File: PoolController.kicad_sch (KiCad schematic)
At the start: 18 parts, among them J1 RJ12, J2 RJ12, J3 Header, J4 Conn_02x12_Counter_Clockwise, Q1 MMBT3904, U1 LM2678S-5.0/NOPB

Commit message: Add revision 15 RX clamp and TX drive prototype package
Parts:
- added D3: BAT54, Package_TO_SOT_SMD:SOT-23, symbol PoolController:BAT54
- J1, J2: footprint Connector_RJ:RJ25_RJ12_5324_mini -> PoolController:RJ12_5324_6P6C
- L1: MPN NPI105C121MTRF or SRR1050A-121Y -> SRR1050A-121Y; Manufacturer NIC Components or Bournes Inc. -> Bourns
- R3: value R1k -> R560; MPN RC0603FR-071KL -> RC0603FR-07560RL
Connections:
- net RX: now reaches J3.2 (Pin_2), J4.5 (Pin_5), R1.2, R2.1
- net RX: now also D3.1 (A)
- net +3V3_MODULE: now reaches J4.3 (Pin_3)
- net +3V3_MODULE: now also D3.3 (K)
- no-connect marks 22 -> 21
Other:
- note added: "RX protection (issue #3) Cathode to Waveshare 3V3 (J4.3). Module must be fitted and powered. Validate powered-off / rail-injection behavior."
- note removed: "+5v"
- note removed: "GND"
- note removed: "RX"
- note removed: "TX"
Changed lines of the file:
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@@
 	(title_block
 		(title "Connect 10 Controller")
-		(date "2026-08-01")
-		(rev "14")
-	)
-	(text "+5v"
-		(exclude_from_sim no)
-		(at 141.478 83.82 0)
-		(effects
-			(font
-				(size 1.27 1.27)
-			)
-		)
-	)
-	(text "GND"
-		(exclude_from_sim no)
-		(at 141.224 86.614 0)
-		(effects
-			(font
-				(size 1.27 1.27)
-			)
-		)
-	)
-	(text "TX"
-		(exclude_from_sim no)
-		(at 142.24 96.774 0)
-		(effects
-			(font
-				(size 1.27 1.27)
-			)
-		)
-	)
-	(text "RX"
-		(exclude_from_sim no)
-		(at 142.24 94.234 0)
-		(effects
-			(font
-				(size 1.27 1.27)
-			)
-		)
+		(date "2026-09-12")
+		(rev "15")
 	)
 	(junction
@@
 	)
 	(no_connect
-		(at 148.59 93.98)
-	)
-	(no_connect
 		(at 161.29 93.98)
 	)
@@
 			)
 		)
-		(property "MPN" "NPI105C121MTRF or SRR1050A-121Y"
+		(property "MPN" "SRR1050A-121Y"
 			(at 138.43 62.23 0)
 			(effects
@@
 			)
 		)
-		(property "Manufacturer" "NIC Components or Bournes Inc."
+		(property "Manufacturer" "Bourns"
 			(at 138.43 62.23 0)
 			(effects
@@
 				)
 				(justify left)
+				(hide yes)
 			)
 		)
@@
 					(size 1.27 1.27)
 				)
+				(hide yes)
 			)
 		)
@@
 			)
 		)
-		(property "Value" "R1k"
+		(property "Value" "R560"
 			(at 140.97 110.4899 0)
 			(effects
@@
 			)
 		)
-		(property "MPN" "RC0603FR-071KL"
+		(property "MPN" "RC0603FR-07560RL"
 			(at 138.43 109.22 0)
 			(effects
@@
 			)
 		)
-		(property "Footprint" "Connector_RJ:RJ25_RJ12_5324_mini"
+		(property "Footprint" "PoolController:RJ12_5324_6P6C"
 			(at 48.26 130.175 90)
 			(effects
@@
 			)
 		)
-		(property "Footprint" "Connector_RJ:RJ25_RJ12_5324_mini"
+		(property "Footprint" "PoolController:RJ12_5324_6P6C"
 			(at 48.26 98.425 90)
 			(effects
@@
 	)
 	(embedded_fonts no)
+	(symbol
+		(lib_id "PoolController:BAT54")
+		(at 182.88 99.06 270)
+		(unit 1)
+		(exclude_from_sim no)
+		(in_bom yes)
+		(on_board yes)
+		(dnp no)
+		(fields_autoplaced yes)
+		(property "Reference" "D3"
+			(at 186.69 96.52 90)
+			(effects
+				(font
+					(size 1.27 1.27)
+				)
+			)
+		)
+		(property "Value" "BAT54"
+			(at 186.69 99.06 90)
+			(effects
+				(font
+					(size 1.27 1.27)
+				)
+			)
+		)
+		(property "Footprint" "Package_TO_SOT_SMD:SOT-23"
+			(at 186.69 99.06 90)
+			(effects
+				(font
+					(size 1.27 1.27)
+				)
+				(hide yes)
+			)
+		)
+		(property "Datasheet" "https://assets.nexperia.com/documents/data-sheet/BAT54.pdf"
+			(at 186.69 99.06 90)
+			(effects
+				(font
+					(size 1.27 1.27)
+				)
+				(hide yes)
+			)
+		)
+		(property "Description" "RX clamp to module 3.3 V; fit module before powering"
+			(at 186.69 99.06 90)
+			(effects
+				(font
+					(size 1.27 1.27)
+				)
+				(hide yes)
+			)
+		)
+		(property "MPN" "BAT54,215"
+			(at 186.69 99.06 90)
+			(effects
+				(font
+					(size 1.27 1.27)
+				)
+				(hide yes)
+			)
+		)
+		(property "Manufacturer" "Nexperia"
+			(at 186.69 99.06 90)
+			(effects
+				(font
+					(size 1.27 1.27)
+				)
+				(hide yes)
+			)
+		)
+		(pin "1"
+		)
+		(pin "2"
+		)
+		(pin "3"
+		)
+		(instances
+			(project "PoolController"
+				(path "/19c01251-b544-42b5-958c-1f3f3624b74e"
+					(reference "D3")
+					(unit 1)
+				)
+			)
+		)
+	)
+	(wire
+		(pts
+			(xy 148.59 93.98)
+			(xy 137.16 93.98)
+		)
+		(stroke
+			(width 0)
+			(type default)
+		)
+	)
+	(label "+3V3_MODULE"
+		(at 137.16 93.98 0)
+		(effects
+			(font
+				(size 1.27 1.27)
+			)
+			(justify left bottom)
+		)
+	)
+	(label "RX"
+		(at 93.98 109.22 0)
+		(effects
+			(font
+				(size 1.27 1.27)
+			)
+			(justify left bottom)
+		)
+	)
+	(wire
+		(pts
+			(xy 182.88 95.25)
+			(xy 182.88 91.44)
+		)
+		(stroke
+			(width 0)
+			(type default)
+		)
+	)
+	(label "+3V3_MODULE"
+		(at 182.88 91.44 0)
+		(effects
+			(font
+				(size 1.27 1.27)
+			)
+			(justify left bottom)
+		)
+	)
+	(wire
+		(pts
+			(xy 182.88 102.87)
+			(xy 182.88 107.95)
+		)
+		(stroke
+			(width 0)
+			(type default)
+		)
+	)
+	(label "RX"
+		(at 182.88 107.95 0)
+		(effects
+			(font
+				(size 1.27 1.27)
+			)
+			(justify left bottom)
+		)
+	)
+	(text "RX protection (issue #3)\nCathode to Waveshare 3V3 (J4.3).\nModule must be fitted and powered.\nValidate powered-off / rail-injection behavior."
+		(at 180.34 115.57 0)
+		(effects
+			(font
+				(size 1.27 1.27)
+			)
+			(justify left top)
+		)
+	)
 )

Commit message: Specify stocked RJ12 sockets and prepare PCBWay carrier assembly package
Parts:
- J1, J2: footprint PoolController:RJ12_5324_6P6C -> PoolController:RJ12_Ckmtw_R-RJ11R06P-A000; MPN (none) -> R-RJ11R06P-A000; Manufacturer (none) -> Ckmtw; Supplier (none) -> LCSC; Supplier Part (none) -> C2902699; Supplier URL (none) -> https://www.lcsc.com/product-detail/C2902699.html
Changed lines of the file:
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@@
 			)
 		)
-		(property "Footprint" "PoolController:RJ12_5324_6P6C"
+		(property "Footprint" "PoolController:RJ12_Ckmtw_R-RJ11R06P-A000"
 			(at 48.26 130.175 90)
 			(effects
@@
 			)
 		)
-		(property "Datasheet" "https://www.aliexpress.com/i/1005008617248283.html"
+		(property "Datasheet" "https://www.lcsc.com/datasheet/C2902699.pdf"
 			(at 48.26 130.175 90)
 			(effects
@@
 			)
 		)
-		(property "Manufacturer" ""
+		(property "Manufacturer" "Ckmtw"
 			(at 48.26 130.81 0)
 			(effects
@@
 			)
 		)
-		(property "MPN" ""
+		(property "MPN" "R-RJ11R06P-A000"
 			(at 48.26 130.81 0)
 			(effects
@@
 					(unit 1)
 				)
+			)
+		)
+		(property "Supplier" "LCSC"
+			(at 48.26 130.81 0)
+			(effects
+				(font
+					(size 1.27 1.27)
+				)
+				(hide yes)
+			)
+		)
+		(property "Supplier Part" "C2902699"
+			(at 48.26 130.81 0)
+			(effects
+				(font
+					(size 1.27 1.27)
+				)
+				(hide yes)
+			)
+		)
+		(property "Supplier URL" "https://www.lcsc.com/product-detail/C2902699.html"
+			(at 48.26 130.81 0)
+			(effects
+				(font
+					(size 1.27 1.27)
+				)
+				(hide yes)
 			)
 		)
@@
 			)
 		)
-		(property "Footprint" "PoolController:RJ12_5324_6P6C"
+		(property "Footprint" "PoolController:RJ12_Ckmtw_R-RJ11R06P-A000"
 			(at 48.26 98.425 90)
 			(effects
@@
 			)
 		)
-		(property "Datasheet" "https://www.aliexpress.com/i/1005008617248283.html"
+		(property "Datasheet" "https://www.lcsc.com/datasheet/C2902699.pdf"
 			(at 48.26 98.425 90)
 			(effects
@@
 			)
 		)
-		(property "Manufacturer" ""
+		(property "Manufacturer" "Ckmtw"
 			(at 48.26 99.06 0)
 			(effects
@@
 			)
 		)
-		(property "MPN" ""
+		(property "MPN" "R-RJ11R06P-A000"
 			(at 48.26 99.06 0)
 			(effects
@@
 			)
 		)
+		(property "Supplier" "LCSC"
+			(at 48.26 99.06 0)
+			(effects
+				(font
+					(size 1.27 1.27)
+				)
+				(hide yes)
+			)
+		)
+		(property "Supplier Part" "C2902699"
+			(at 48.26 99.06 0)
+			(effects
+				(font
+					(size 1.27 1.27)
+				)
+				(hide yes)
+			)
+		)
+		(property "Supplier URL" "https://www.lcsc.com/product-detail/C2902699.html"
+			(at 48.26 99.06 0)
+			(effects
+				(font
+					(size 1.27 1.27)
+				)
+				(hide yes)
+			)
+		)

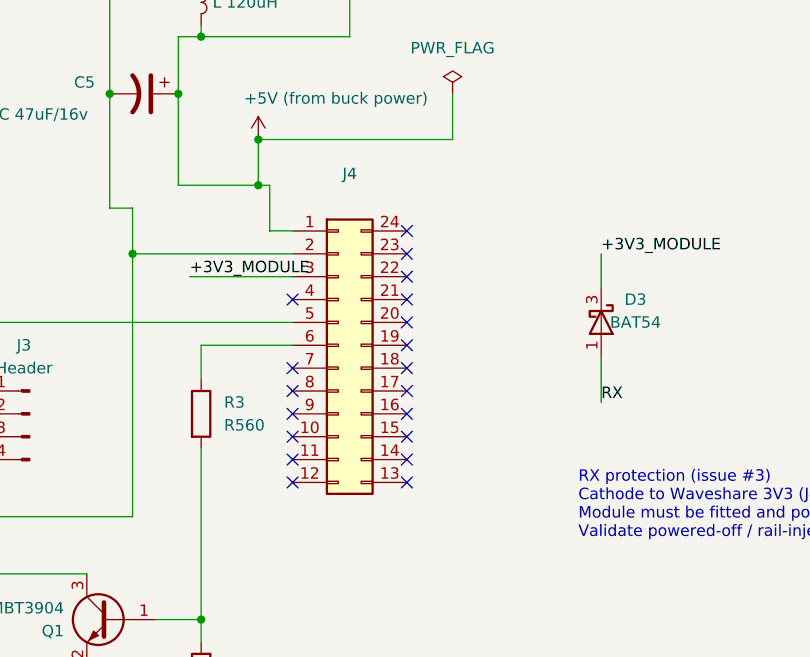
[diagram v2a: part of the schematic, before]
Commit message: Replace legacy carrier parts and preserve enclosure mounting fit
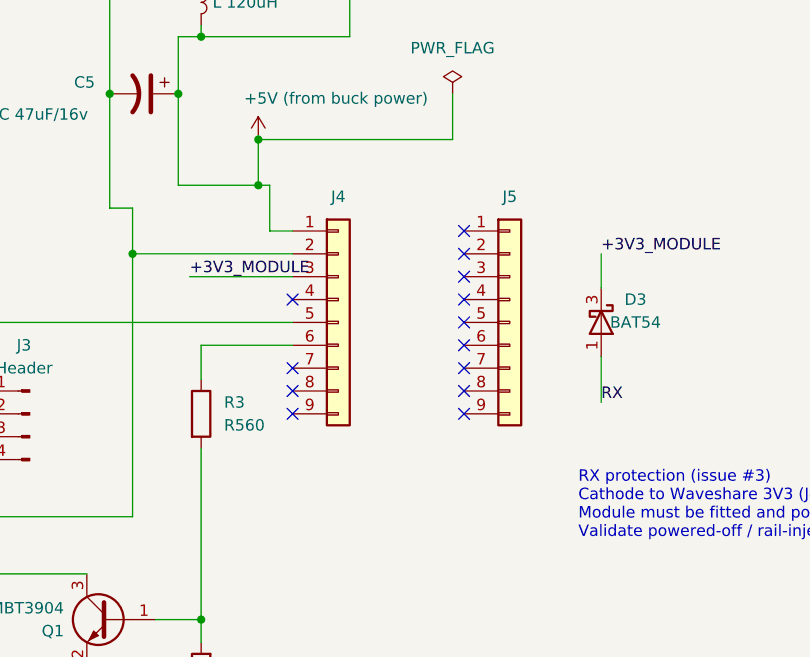
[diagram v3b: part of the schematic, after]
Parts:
- added J5: SSW-109-01-T-S, PoolController:Samtec_SSW-109-01-T-S_1x09, symbol Connector_Generic:Conn_01x09
- C1: MPN C2012C0G1H103K060AA -> C2012C0G1H103J060AA
- C2, C3: MPN GRM32ER71J106KA12L -> CL32B106KMVNNWE; Manufacturer MuRata -> Samsung Electro-Mechanics
- C5: MPN GRM32ER61C476KE15L -> CL32A476KOJNNNE; Manufacturer MuRata -> Samsung Electro-Mechanics
- J4: value Conn_02x12_Counter_Clockwise -> SSW-109-01-T-S; footprint Package_DIP:DIP-24_18.0mmx34.29mm_W15.24mm_Socket -> PoolController:Samtec_SSW-109-01-T-S_1x09; symbol Connector_Generic:Conn_02x12_Counter_Clockwise -> Connector_Generic:Conn_01x09; MPN DILB24P-223TLF -> SSW-109-01-T-S; Manufacturer Amphenol ICC (FCI) -> Samtec
- L1: MPN SRR1050A-121Y -> SRR1050HA-121Y
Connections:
- no-connect marks 21 -> 15
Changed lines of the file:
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@@
 	)
 	(no_connect
-		(at 161.29 101.6)
-	)
-	(no_connect
 		(at 148.59 104.14)
 	)
 	(no_connect
-		(at 161.29 111.76)
-	)
-	(no_connect
 		(at 151.13 36.83)
 	)
@@
 	)
 	(no_connect
-		(at 161.29 116.84)
-	)
-	(no_connect
-		(at 161.29 88.9)
-	)
-	(no_connect
-		(at 161.29 93.98)
-	)
-	(no_connect
-		(at 161.29 114.3)
-	)
-	(no_connect
 		(at 151.13 41.91)
 	)
 	(no_connect
-		(at 161.29 99.06)
-	)
-	(no_connect
-		(at 161.29 109.22)
-	)
-	(no_connect
-		(at 161.29 104.14)
-	)
-	(no_connect
-		(at 148.59 111.76)
-	)
-	(no_connect
-		(at 161.29 96.52)
-	)
-	(no_connect
-		(at 161.29 106.68)
-	)
-	(no_connect
-		(at 161.29 91.44)
-	)
-	(no_connect
-		(at 148.59 114.3)
-	)
-	(no_connect
 		(at 148.59 109.22)
 	)
-	(no_connect
-		(at 148.59 116.84)
-	)
 	(wire
 		(pts
@@
 			)
 		)
-		(property "Datasheet" "~"
+		(property "Datasheet" "https://www.bourns.com/docs/product-datasheets/srr1050ha.pdf"
 			(at 138.43 62.23 0)
 			(effects
@@
 			)
 		)
-		(property "MPN" "SRR1050A-121Y"
+		(property "MPN" "SRR1050HA-121Y"
 			(at 138.43 62.23 0)
 			(effects
@@
 			)
 		)
-		(property "Datasheet" "~"
+		(property "Datasheet" "https://weblib.samsungsem.com/mlcc/mlcc-ec-data-sheet.do?partNumber=CL32B106KMVNNW"
 			(at 87.63 64.77 0)
 			(effects
@@
 			)
 		)
-		(property "MPN" "GRM32ER71J106KA12L"
+		(property "MPN" "CL32B106KMVNNWE"
 			(at 87.63 64.77 90)
 			(effects
@@
 			)
 		)
-		(property "Manufacturer" "MuRata"
+		(property "Manufacturer" "Samsung Electro-Mechanics"
 			(at 87.63 64.77 90)
 			(effects
@@
 			)
 		)
-		(property "Datasheet" "~"
+		(property "Datasheet" "https://product.tdk.com/en/search/capacitor/ceramic/mlcc/info?part_no=C2012C0G1H103J060AA"
 			(at 64.77 39.37 0)
 			(effects
@@
 			)
 		)
-		(property "MPN" "C2012C0G1H103K060AA"
+		(property "MPN" "C2012C0G1H103J060AA"
 			(at 64.77 39.37 0)
 			(effects
@@
 	)
 	(symbol
-		(lib_id "Connector_Generic:Conn_02x12_Counter_Clockwise")
-		(at 153.67 101.6 0)
+		(lib_id "Connector_Generic:Conn_01x09")
+		(at 153.67 99.06 0)
 		(unit 1)
 		(exclude_from_sim no)
@@
 		(fields_autoplaced yes)
 		(property "Reference" "J4"
-			(at 154.94 82.55 0)
+			(at 153.67 85.09 0)
 			(effects
 				(font
@@
 			)
 		)
-		(property "Value" "Conn_02x12_Counter_Clockwise"
+		(property "Value" "SSW-109-01-T-S"
 			(at 154.94 85.09 0)
 			(effects
@@
 			)
 		)
-		(property "Footprint" "Package_DIP:DIP-24_18.0mmx34.29mm_W15.24mm_Socket"
+		(property "Footprint" "PoolController:Samtec_SSW-109-01-T-S_1x09"
 			(at 153.67 101.6 0)
 			(effects
@@
 			)
 		)
-		(property "Datasheet" "~"
+		(property "Datasheet" "https://suddendocs.samtec.com/prints/ssw-s.pdf"
 			(at 153.67 101.6 0)
 			(effects
@@
 			)
 		)
-		(property "Description" "Generic connector, double row, 02x12, counter clockwise pin numbering scheme (similar to DIP package numbering), script generated (kicad-library-utils/schlib/autogen/connector/)"
+		(property "Description" "Samtec nine-position female header for Waveshare module"
 			(at 153.67 101.6 0)
 			(effects
@@
 			)
 		)
-		(property "Manufacturer" "Amphenol ICC (FCI)"
+		(property "Manufacturer" "Samtec"
 			(at 153.67 101.6 0)
 			(effects
@@
 			)
 		)
-		(property "MPN" "DILB24P-223TLF"
+		(property "MPN" "SSW-109-01-T-S"
 			(at 153.67 101.6 0)
 			(effects
@@
 			)
 		)
-		(pin "19"
-		)
-		(pin "20"
-		)
-		(pin "21"
-		)
-		(pin "22"
-		)
-		(pin "13"
-		)
-		(pin "14"
-		)
-		(pin "15"
-		)
-		(pin "16"
-		)
-		(pin "17"
-		)
-		(pin "18"
-		)
-		(pin "10"
-		)
-		(pin "12"
-		)
 		(pin "9"
 		)
-		(pin "23"
-		)
-		(pin "11"
-		)
 		(pin "2"
 		)
-		(pin "24"
-		)
 		(pin "5"
 		)
@@
 			)
 		)
-		(property "Datasheet" "~"
+		(property "Datasheet" "https://product.samsungsem.com/mlcc/CL32A476KOJNNN.do"
 			(at 132.08 73.66 0)
 			(effects
@@
 			)
 		)
-		(property "MPN" "GRM32ER61C476KE15L"
+		(property "MPN" "CL32A476KOJNNNE"
 			(at 132.08 73.66 90)
 			(effects
@@
 			)
 		)
-		(property "Manufacturer" "MuRata"
+		(property "Manufacturer" "Samsung Electro-Mechanics"
 			(at 132.08 73.66 90)
 			(effects
@@
 			)
 		)
-		(property "Datasheet" "~"
+		(property "Datasheet" "https://weblib.samsungsem.com/mlcc/mlcc-ec-data-sheet.do?partNumber=CL32B106KMVNNW"
 			(at 87.63 72.39 0)
 			(effects
@@
 			)
 		)
-		(property "MPN" "GRM32ER71J106KA12L"
+		(property "MPN" "CL32B106KMVNNWE"
 			(at 87.63 72.39 90)
 			(effects
@@
 			)
 		)
-		(property "Manufacturer" "MuRata"
+		(property "Manufacturer" "Samsung Electro-Mechanics"
 			(at 87.63 72.39 90)
 			(effects
@@
 		)
 	)
+(symbol
+		(lib_id "Connector_Generic:Conn_01x09")
+		(at 172.72 99.06 0)
+		(unit 1)
+		(exclude_from_sim no)
+		(in_bom yes)
+		(on_board yes)
+		(dnp no)
+		(fields_autoplaced yes)
+		(property "Reference" "J5"
+			(at 172.72 85.09 0)
+			(effects
+				(font
+					(size 1.27 1.27)
+				)
+			)
+		)
+		(property "Value" "SSW-109-01-T-S"
+			(at 172.72 85.09 0)
+			(effects
+				(font
+					(size 1.27 1.27)
+				)
+				(hide yes)
+			)
+		)
+		(property "Footprint" "PoolController:Samtec_SSW-109-01-T-S_1x09"
+			(at 172.72 101.6 0)
+			(effects
+				(font
+					(size 1.27 1.27)
+				)
+				(hide yes)
+			)
+		)
+		(property "Datasheet" "https://suddendocs.samtec.com/prints/ssw-s.pdf"
+			(at 172.72 101.6 0)
+			(effects
+				(font
+					(size 1.27 1.27)
+				)
+				(hide yes)
+			)
+		)
+		(property "Description" "Samtec nine-position female header for Waveshare module"
+			(at 172.72 101.6 0)
+			(effects
+				(font
+					(size 1.27 1.27)
+				)
+				(hide yes)
+			)
+		)
+		(property "Manufacturer" "Samtec"
+			(at 172.72 101.6 0)
+			(effects
+				(font
+					(size 1.27 1.27)
+				)
+				(hide yes)
+			)
+		)
+		(property "MPN" "SSW-109-01-T-S"
+			(at 172.72 101.6 0)
+			(effects
+				(font
+					(size 1.27 1.27)
+				)
+				(hide yes)
+			)
+		)
+		(pin "9"
+		)
+		(pin "2"
+		)
+		(pin "5"
+		)
+		(pin "6"
+		)
+		(pin "3"
+		)
+		(pin "8"
+		)
+		(pin "4"
+		)
+		(pin "1"
+		)
+		(pin "7"
+		)
+		(instances
+			(project ""
+				(path "/19c01251-b544-42b5-958c-1f3f3624b74e"
+					(reference "J5")
+					(unit 1)
+				)
+			)
+		)
+	)
+(no_connect
+		(at 167.64 88.90)
+	)
+(no_connect
+		(at 167.64 91.44)
+	)
+(no_connect
+		(at 167.64 93.98)
+	)
+(no_connect
+		(at 167.64 96.52)
+	)
+(no_connect
+		(at 167.64 99.06)
+	)
+(no_connect
+		(at 167.64 101.60)
+	)
+(no_connect
+		(at 167.64 104.14)
+	)
+(no_connect
+		(at 167.64 106.68)
+	)
+(no_connect
+		(at 167.64 109.22)
+	)
 )
